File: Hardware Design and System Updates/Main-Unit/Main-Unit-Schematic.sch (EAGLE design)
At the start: 16 parts, among them U1 MSP430FR2110IPW16, U2 TLR342F-GE2SOP8_ROM, U3 L7805CV, U4 TMP36GT9ZT_3_ADI

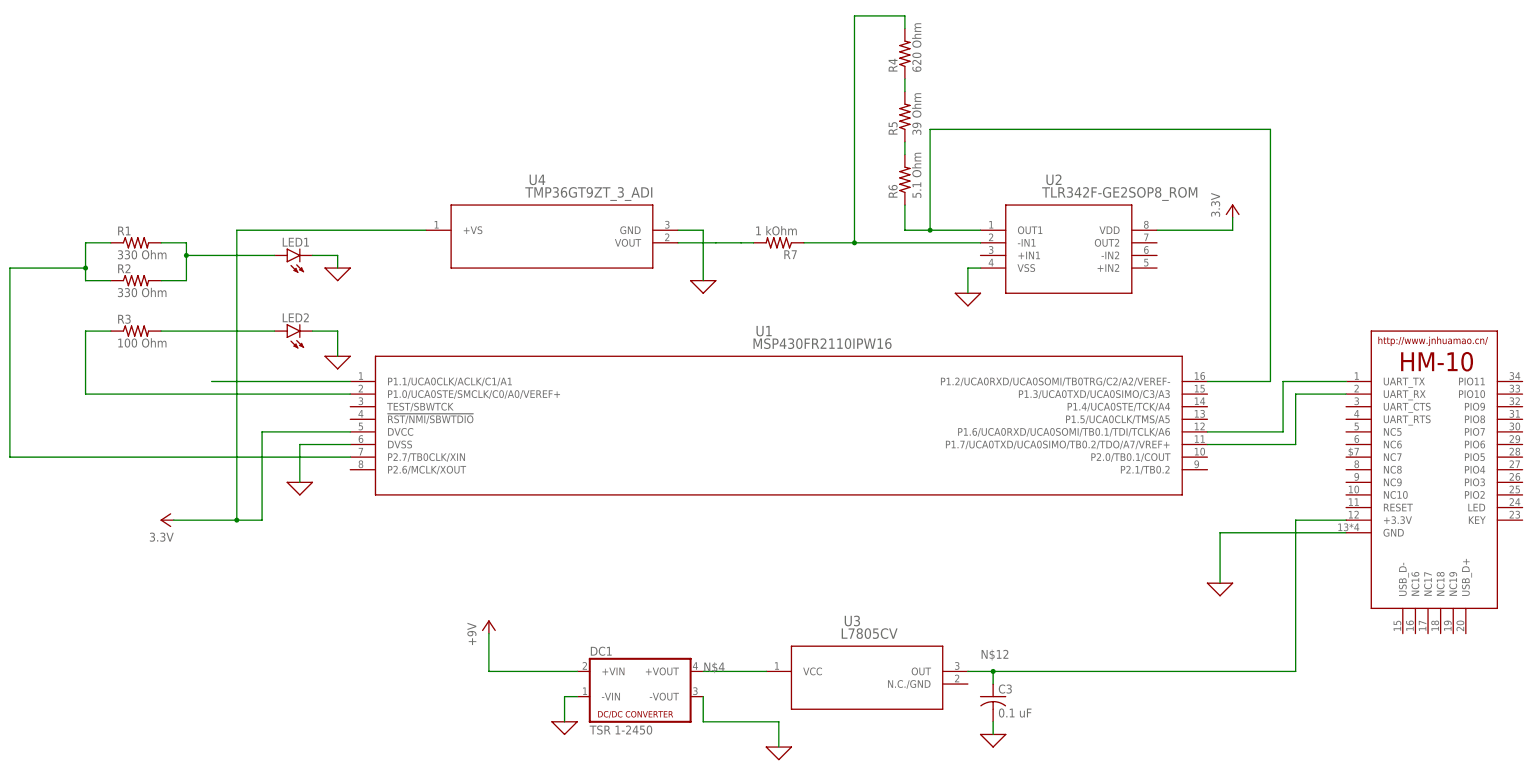
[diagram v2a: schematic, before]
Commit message: Fixed system schematics
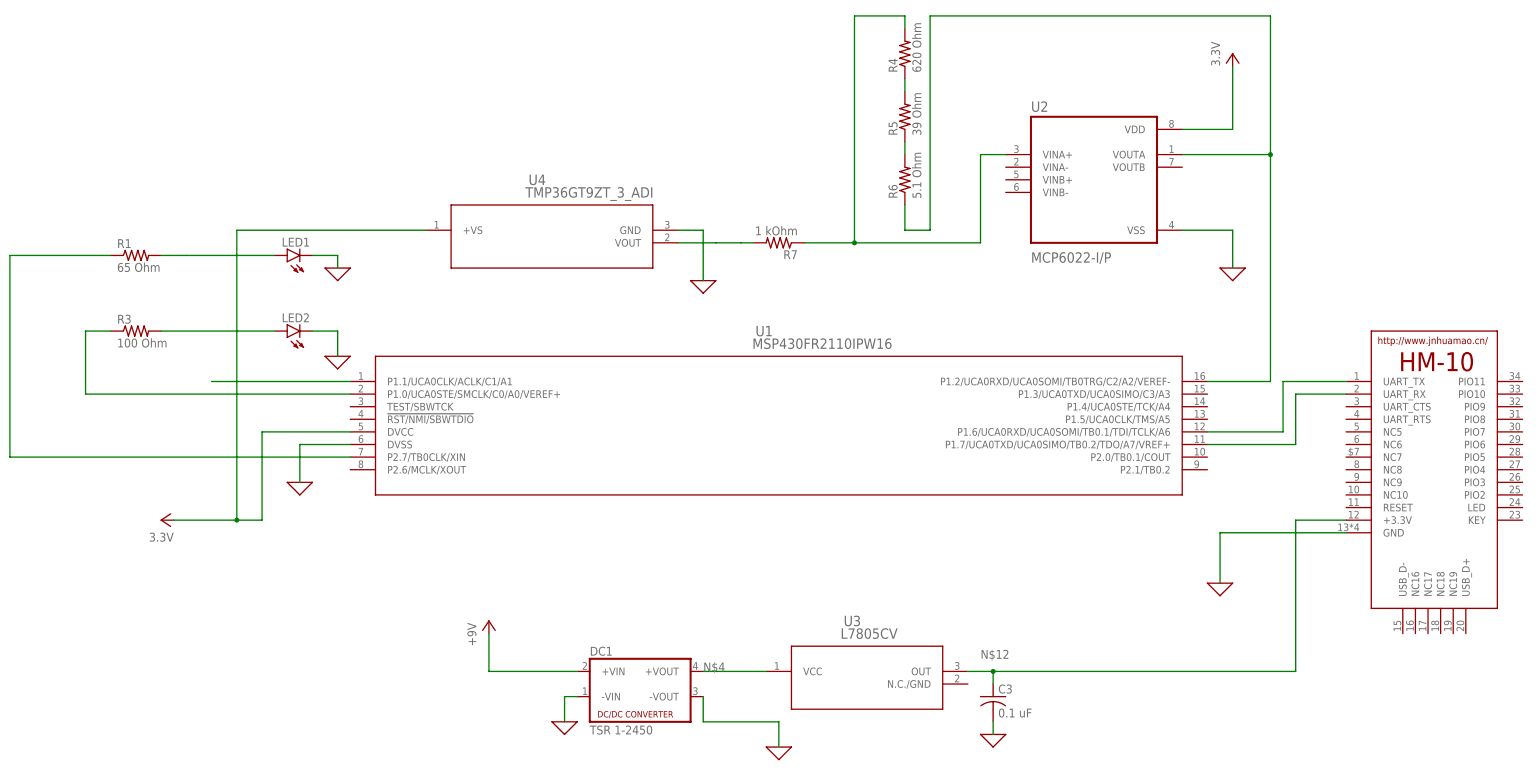
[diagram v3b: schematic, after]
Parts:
- removed R2: 330 Ohm, rcl:R-US_0204/7
- R1: value 330 Ohm -> 65 Ohm
- U2: value TLR342F-GE2SOP8_ROM -> MCP6022-I/P; device 2023-03-28_11-48-47_Library:TLR342F-GE2SOP8_ROM -> MCP6022-I_P:MCP6022-I/P
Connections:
- net N$10: now also U2.VOUTA; no longer U2.OUT1
- net N$11: now also U2.VINA+; no longer U2.-IN1
- net N$4: no longer R2.1
- net N$6: no longer R2.2
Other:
- moved on the sheet: R1, U2
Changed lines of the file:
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@@
 <part name="LED1" library="led" library_urn="urn:adsk.eagle:library:259" deviceset="LED" device="5MM" package3d_urn="urn:adsk.eagle:package:15799/2"/>
 <part name="LED2" library="led" library_urn="urn:adsk.eagle:library:259" deviceset="LED" device="5MM" package3d_urn="urn:adsk.eagle:package:15799/2"/>
-<part name="R1" library="rcl" library_urn="urn:adsk.eagle:library:334" deviceset="R-US_" device="0204/7" package3d_urn="urn:adsk.eagle:package:23498/2" value="330 Ohm"/>
-<part name="R2" library="rcl" library_urn="urn:adsk.eagle:library:334" deviceset="R-US_" device="0204/7" package3d_urn="urn:adsk.eagle:package:23498/2" value="330 Ohm"/>
+<part name="R1" library="rcl" library_urn="urn:adsk.eagle:library:334" deviceset="R-US_" device="0204/7" package3d_urn="urn:adsk.eagle:package:23498/2" value="65 Ohm"/>
 <part name="R3" library="rcl" library_urn="urn:adsk.eagle:library:334" deviceset="R-US_" device="0204/7" package3d_urn="urn:adsk.eagle:package:23498/2" value="100 Ohm"/>
 <part name="X_3" library="ngspice-simulation" library_urn="urn:adsk.eagle:library:527439" deviceset="GND" device=""/>
 <part name="X_4" library="ngspice-simulation" library_urn="urn:adsk.eagle:library:527439" deviceset="GND" device=""/>
-<part name="U2" library="2023-03-28_11-48-47_Library" deviceset="TLR342F-GE2" device="SOP8_ROM"/>
 <part name="P+2" library="supply1" library_urn="urn:adsk.eagle:library:371" deviceset="VCC" device="" value="3.3V"/>
 <part name="X_5" library="ngspice-simulation" library_urn="urn:adsk.eagle:library:527439" deviceset="GND" device=""/>
@@
 <part name="X_10" library="ngspice-simulation" library_urn="urn:adsk.eagle:library:527439" deviceset="GND" device=""/>
 <part name="P+3" library="supply1" library_urn="urn:adsk.eagle:library:371" deviceset="+5V" device="" value="+9V"/>
+<part name="U2" library="MCP6022-I_P" deviceset="MCP6022-I/P" device=""/>
 </parts>
 <sheets>
@@
 <attribute name="VALUE" x="-10.668" y="76.835" size="1.778" layer="96" rot="R180"/>
 </instance>
-<instance part="R1" gate="G$1" x="-45.72" y="88.9" smashed="yes">
-<attribute name="NAME" x="-49.53" y="90.3986" size="1.778" layer="95"/>
-<attribute name="VALUE" x="-49.53" y="85.598" size="1.778" layer="96"/>
-</instance>
-<instance part="R2" gate="G$1" x="-45.72" y="81.28" smashed="yes">
-<attribute name="NAME" x="-49.53" y="82.7786" size="1.778" layer="95"/>
-<attribute name="VALUE" x="-49.53" y="77.978" size="1.778" layer="96"/>
+<instance part="R1" gate="G$1" x="-45.72" y="86.36" smashed="yes">
+<attribute name="NAME" x="-49.53" y="87.8586" size="1.778" layer="95"/>
+<attribute name="VALUE" x="-49.53" y="83.058" size="1.778" layer="96"/>
 </instance>
 <instance part="R3" gate="G$1" x="-45.72" y="71.12" smashed="yes">
@@
 <instance part="X_3" gate="G$1" x="-5.08" y="66.04" smashed="yes"/>
 <instance part="X_4" gate="G$1" x="-5.08" y="83.82" smashed="yes"/>
-<instance part="U2" gate="A" x="121.92" y="91.44" smashed="yes">
-<attribute name="NAME" x="137.5146" y="100.5586" size="2.083" layer="95" ratio="6"/>
-<attribute name="VALUE" x="136.8752" y="98.0186" size="2.083" layer="96" ratio="6"/>
-</instance>
-<instance part="P+2" gate="VCC" x="175.26" y="96.52" smashed="yes">
-<attribute name="VALUE" x="172.72" y="93.98" size="1.778" layer="96" rot="R90"/>
-</instance>
-<instance part="X_5" gate="G$1" x="121.92" y="78.74" smashed="yes"/>
+<instance part="P+2" gate="VCC" x="175.26" y="127" smashed="yes">
+<attribute name="VALUE" x="172.72" y="124.46" size="1.778" layer="96" rot="R90"/>
+</instance>
+<instance part="X_5" gate="G$1" x="175.26" y="83.82" smashed="yes"/>
 <instance part="R4" gate="G$1" x="109.22" y="127" smashed="yes" rot="R90">
 <attribute name="NAME" x="107.7214" y="123.19" size="1.778" layer="95" rot="R90"/>
@@
 <instance part="P+3" gate="1" x="25.4" y="12.7" smashed="yes">
 <attribute name="VALUE" x="22.86" y="7.62" size="1.778" layer="96" rot="R90"/>
+</instance>
+<instance part="U2" gate="A" x="147.32" y="101.6" smashed="yes">
+<attribute name="NAME" x="134.62" y="115.3" size="2.0828" layer="95" ratio="10" rot="SR0"/>
+<attribute name="VALUE" x="134.62" y="84.9" size="2.0828" layer="96" ratio="10" rot="SR0"/>
 </instance>
 </instances>
@@
 <segment>
 <pinref part="U2" gate="A" pin="VDD"/>
-<wire x1="160.02" y1="91.44" x2="175.26" y2="91.44" width="0.1524" layer="91"/>
+<wire x1="165.1" y1="111.76" x2="175.26" y2="111.76" width="0.1524" layer="91"/>
 <pinref part="P+2" gate="VCC" pin="VCC"/>
-<wire x1="175.26" y1="91.44" x2="175.26" y2="93.98" width="0.1524" layer="91"/>
+<wire x1="175.26" y1="111.76" x2="175.26" y2="124.46" width="0.1524" layer="91"/>
 </segment>
 </net>
@@
 <pinref part="X_3" gate="G$1" pin="0"/>
 <wire x1="-5.08" y1="71.12" x2="-5.08" y2="66.04" width="0.1524" layer="91"/>
-</segment>
-<segment>
-<pinref part="X_5" gate="G$1" pin="0"/>
-<pinref part="U2" gate="A" pin="VSS"/>
-<wire x1="121.92" y1="78.74" x2="121.92" y2="83.82" width="0.1524" layer="91"/>
-<wire x1="121.92" y1="83.82" x2="124.46" y2="83.82" width="0.1524" layer="91"/>
 </segment>
 <segment>
@@
 <wire x1="127" y1="-10.16" x2="127" y2="-7.62" width="0.1524" layer="91"/>
 </segment>
+<segment>
+<pinref part="U2" gate="A" pin="VSS"/>
+<pinref part="X_5" gate="G$1" pin="0"/>
+<wire x1="165.1" y1="91.44" x2="175.26" y2="91.44" width="0.1524" layer="91"/>
+<wire x1="175.26" y1="91.44" x2="175.26" y2="83.82" width="0.1524" layer="91"/>
+</segment>
 </net>
 <net name="N$3" class="0">
@@
 <net name="N$4" class="0">
 <segment>
-<pinref part="R2" gate="G$1" pin="1"/>
-<wire x1="-50.8" y1="81.28" x2="-55.88" y2="81.28" width="0.1524" layer="91"/>
+<pinref part="U1" gate="A" pin="P2.7/TB0CLK/XIN"/>
+<wire x1="-71.12" y1="86.36" x2="-71.12" y2="45.72" width="0.1524" layer="91"/>
+<wire x1="-71.12" y1="45.72" x2="-2.54" y2="45.72" width="0.1524" layer="91"/>
 <pinref part="R1" gate="G$1" pin="1"/>
-<wire x1="-55.88" y1="81.28" x2="-55.88" y2="83.82" width="0.1524" layer="91"/>
-<wire x1="-55.88" y1="83.82" x2="-55.88" y2="88.9" width="0.1524" layer="91"/>
-<wire x1="-55.88" y1="88.9" x2="-50.8" y2="88.9" width="0.1524" layer="91"/>
-<wire x1="-55.88" y1="83.82" x2="-71.12" y2="83.82" width="0.1524" layer="91"/>
-<junction x="-55.88" y="83.82"/>
-<pinref part="U1" gate="A" pin="P2.7/TB0CLK/XIN"/>
-<wire x1="-71.12" y1="83.82" x2="-71.12" y2="45.72" width="0.1524" layer="91"/>
-<wire x1="-71.12" y1="45.72" x2="-2.54" y2="45.72" width="0.1524" layer="91"/>
+<wire x1="-50.8" y1="86.36" x2="-71.12" y2="86.36" width="0.1524" layer="91"/>
 </segment>
 <segment>
@@
 <net name="N$6" class="0">
 <segment>
-<pinref part="R2" gate="G$1" pin="2"/>
-<wire x1="-40.64" y1="81.28" x2="-35.56" y2="81.28" width="0.1524" layer="91"/>
-<wire x1="-35.56" y1="81.28" x2="-35.56" y2="86.36" width="0.1524" layer="91"/>
+<pinref part="LED1" gate="G$1" pin="A"/>
+<wire x1="-35.56" y1="86.36" x2="-33.02" y2="86.36" width="0.1524" layer="91"/>
 <pinref part="R1" gate="G$1" pin="2"/>
-<wire x1="-35.56" y1="86.36" x2="-35.56" y2="88.9" width="0.1524" layer="91"/>
-<wire x1="-35.56" y1="88.9" x2="-40.64" y2="88.9" width="0.1524" layer="91"/>
-<pinref part="LED1" gate="G$1" pin="A"/>
-<wire x1="-35.56" y1="86.36" x2="-17.78" y2="86.36" width="0.1524" layer="91"/>
-<junction x="-35.56" y="86.36"/>
+<wire x1="-33.02" y1="86.36" x2="-17.78" y2="86.36" width="0.1524" layer="91"/>
+<wire x1="-40.64" y1="86.36" x2="-35.56" y2="86.36" width="0.1524" layer="91"/>
 </segment>
 </net>
@@
 <wire x1="109.22" y1="132.08" x2="109.22" y2="134.62" width="0.1524" layer="91"/>
 <wire x1="109.22" y1="134.62" x2="99.06" y2="134.62" width="0.1524" layer="91"/>
-<pinref part="U2" gate="A" pin="-IN1"/>
 <wire x1="124.46" y1="88.9" x2="99.06" y2="88.9" width="0.1524" layer="91"/>
 <wire x1="99.06" y1="134.62" x2="99.06" y2="88.9" width="0.1524" layer="91"/>
@@
 <wire x1="99.06" y1="88.9" x2="88.9" y2="88.9" width="0.1524" layer="91"/>
 <junction x="99.06" y="88.9"/>
+<wire x1="124.46" y1="88.9" x2="124.46" y2="106.68" width="0.1524" layer="91"/>
+<pinref part="U2" gate="A" pin="VINA+"/>
+<wire x1="124.46" y1="106.68" x2="129.54" y2="106.68" width="0.1524" layer="91"/>
 </segment>
 </net>
@@
 <pinref part="U1" gate="A" pin="P1.2/UCA0RXD/UCA0SOMI/TB0TRG/C2/A2/VEREF-"/>
 <wire x1="182.88" y1="60.96" x2="170.18" y2="60.96" width="0.1524" layer="91"/>
-<pinref part="U2" gate="A" pin="OUT1"/>
-<wire x1="124.46" y1="91.44" x2="114.3" y2="91.44" width="0.1524" layer="91"/>
 <pinref part="R6" gate="G$1" pin="1"/>
 <wire x1="114.3" y1="91.44" x2="109.22" y2="91.44" width="0.1524" layer="91"/>
 <wire x1="109.22" y1="91.44" x2="109.22" y2="96.52" width="0.1524" layer="91"/>
-<wire x1="114.3" y1="91.44" x2="114.3" y2="111.76" width="0.1524" layer="91"/>
-<wire x1="114.3" y1="111.76" x2="182.88" y2="111.76" width="0.1524" layer="91"/>
-<junction x="114.3" y="91.44"/>
-<wire x1="182.88" y1="60.96" x2="182.88" y2="111.76" width="0.1524" layer="91"/>
-</segment>
-</net>
+<wire x1="114.3" y1="91.44" x2="114.3" y2="134.62" width="0.1524" layer="91"/>
+<wire x1="114.3" y1="134.62" x2="182.88" y2="134.62" width="0.1524" layer="91"/>
+<wire x1="182.88" y1="60.96" x2="182.88" y2="106.68" width="0.1524" layer="91"/>
+<pinref part="U2" gate="A" pin="VOUTA"/>
+<wire x1="182.88" y1="106.68" x2="182.88" y2="134.62" width="0.1524" layer="91"/>
+<wire x1="165.1" y1="106.68" x2="182.88" y2="106.68" width="0.1524" layer="91"/>
+<junction x="182.88" y="106.68"/>
+</segment>
+</net>
